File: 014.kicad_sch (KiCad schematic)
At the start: 19 parts, among them J14 USB2.0 Type C, U1 AM6232ASCGHAALWR, U6 TVS0500DRVR

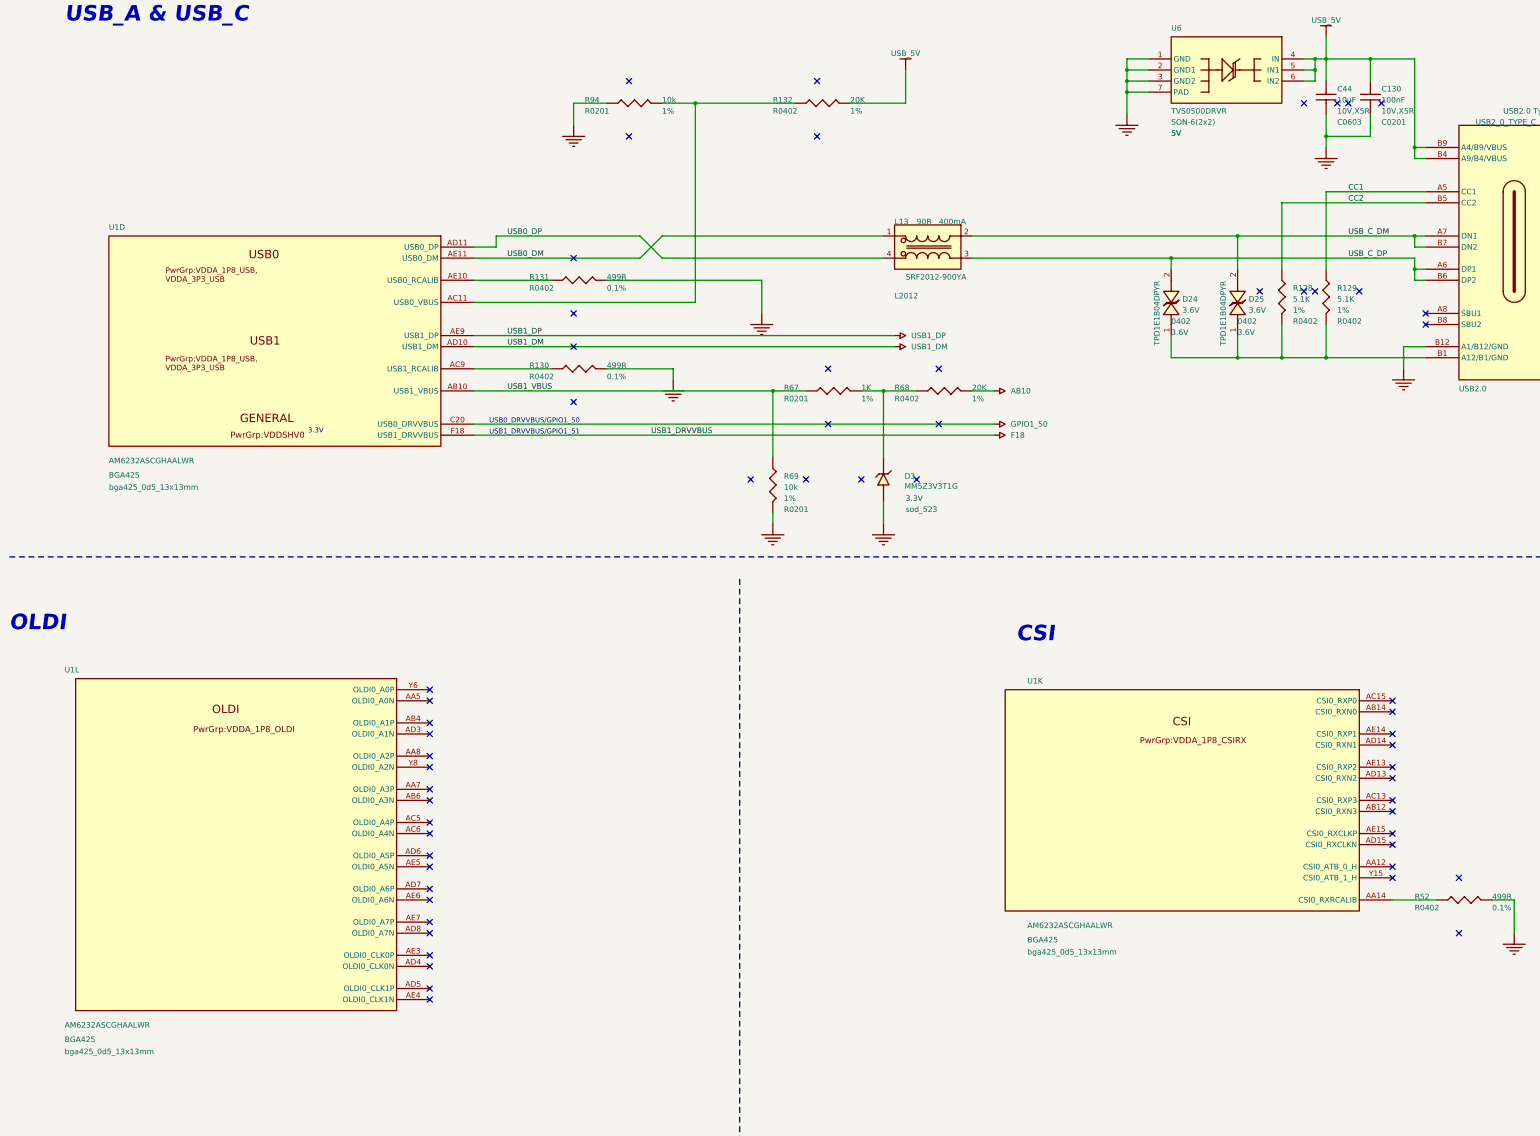
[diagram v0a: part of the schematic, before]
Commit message: Remove rando NCs added during conversion
Also a little tidying.

TODO: check junctions that may be missing. Noticed a few obvious ones
and corrected them already.

Signed-off-by: Michael Welling <mwelling79@gmail.com>
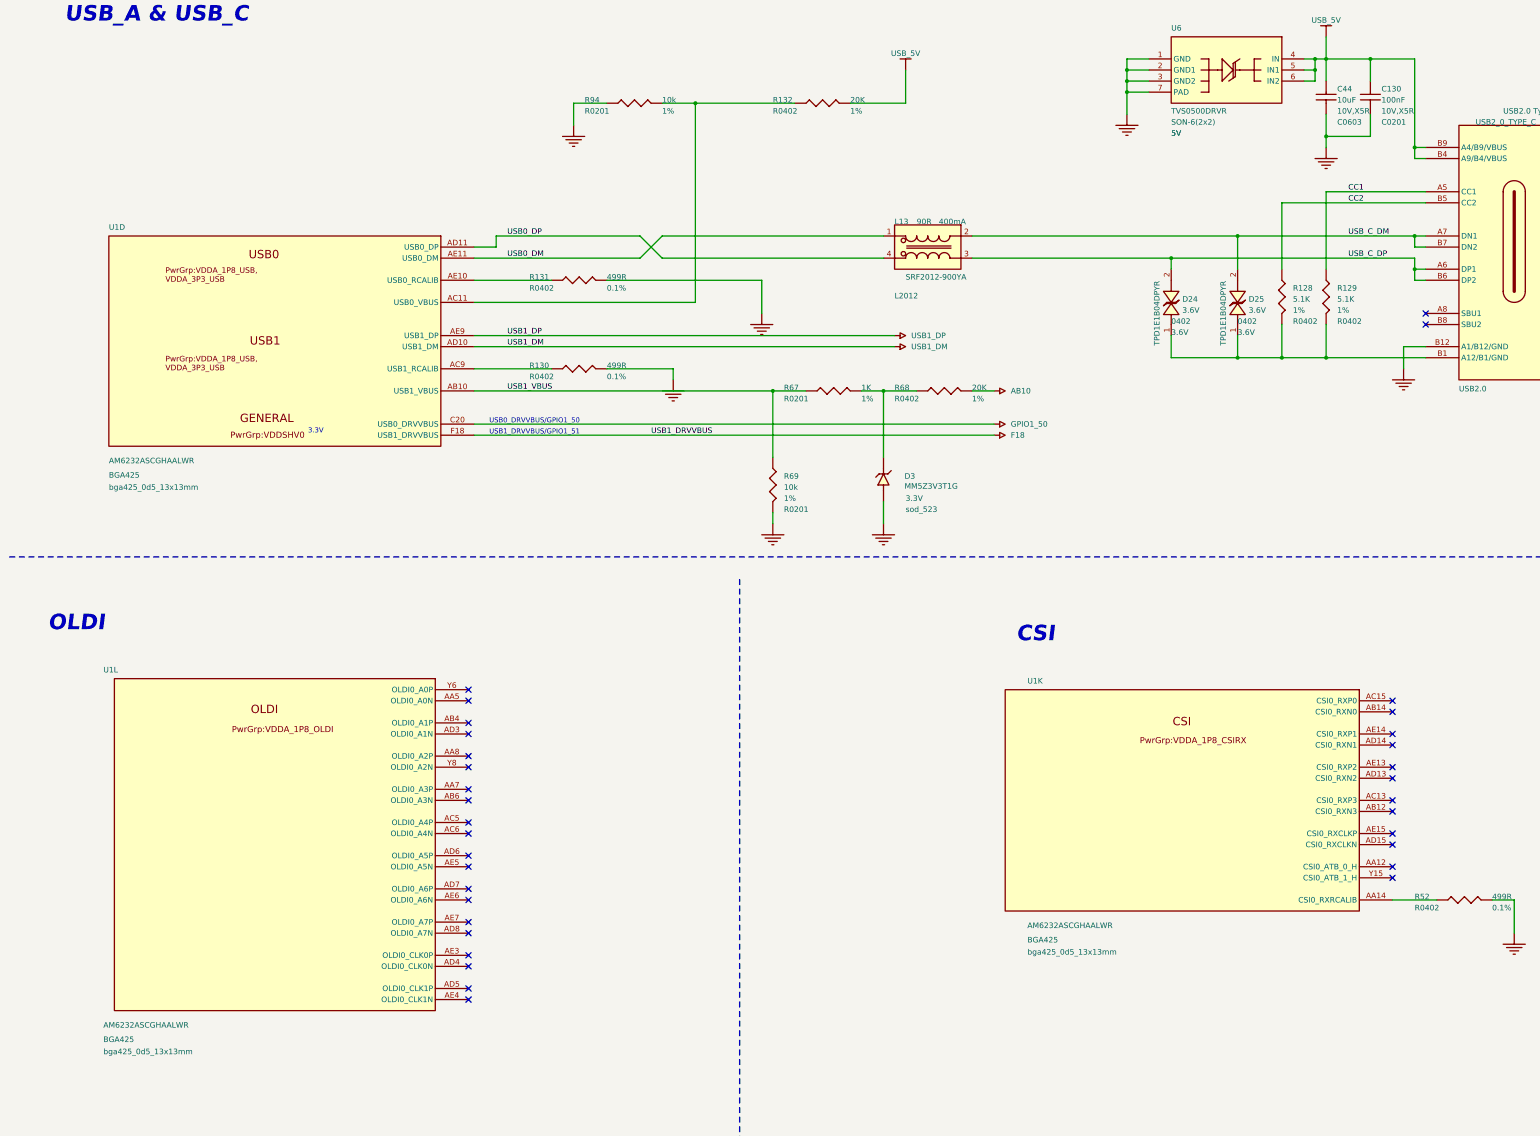
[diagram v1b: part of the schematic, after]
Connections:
- no-connect marks 60 -> 34
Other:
- moved on the sheet: U1L
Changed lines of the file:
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@@
 	)
 	(no_connect
-		(at 149.86 45.72)
-	)
-	(no_connect
-		(at 177.8 124.46)
-	)
-	(no_connect
 		(at 325.12 213.36)
 	)
@@
 	)
 	(no_connect
-		(at 220.98 99.06)
-	)
-	(no_connect
 		(at 325.12 190.5)
 	)
 	(no_connect
-		(at 104.14 180.34)
+		(at 113.03 180.34)
 	)
 	(no_connect
@@
 	)
 	(no_connect
-		(at 104.14 172.72)
+		(at 113.03 172.72)
 	)
 	(no_connect
-		(at 104.14 243.84)
-	)
-	(no_connect
-		(at 137.16 106.68)
+		(at 113.03 243.84)
 	)
 	(no_connect
@@
 	)
 	(no_connect
-		(at 104.14 233.68)
-	)
-	(no_connect
-		(at 340.36 228.6)
+		(at 113.03 233.68)
 	)
 	(no_connect
-		(at 322.58 38.1)
-	)
-	(no_connect
-		(at 104.14 213.36)
+		(at 113.03 213.36)
 	)
 	(no_connect
@@
 	)
 	(no_connect
-		(at 340.36 215.9)
-	)
-	(no_connect
-		(at 195.58 111.76)
-	)
-	(no_connect
-		(at 104.14 205.74)
-	)
-	(no_connect
-		(at 314.96 38.1)
-	)
-	(no_connect
-		(at 304.8 38.1)
+		(at 113.03 205.74)
 	)
 	(no_connect
-		(at 104.14 210.82)
+		(at 113.03 210.82)
 	)
 	(no_connect
-		(at 104.14 175.26)
-	)
-	(no_connect
-		(at 193.04 45.72)
+		(at 113.03 175.26)
 	)
 	(no_connect
@@
 	)
 	(no_connect
-		(at 104.14 198.12)
-	)
-	(no_connect
-		(at 215.9 124.46)
-	)
-	(no_connect
-		(at 220.98 111.76)
+		(at 113.03 198.12)
 	)
 	(no_connect
-		(at 104.14 226.06)
+		(at 113.03 226.06)
 	)
 	(no_connect
-		(at 104.14 182.88)
+		(at 113.03 182.88)
 	)
 	(no_connect
-		(at 104.14 203.2)
+		(at 113.03 203.2)
 	)
 	(no_connect
@@
 	)
 	(no_connect
-		(at 104.14 241.3)
+		(at 113.03 241.3)
 	)
 	(no_connect
-		(at 104.14 220.98)
+		(at 113.03 220.98)
 	)
 	(no_connect
-		(at 137.16 86.36)
+		(at 113.03 187.96)
 	)
 	(no_connect
-		(at 104.14 187.96)
-	)
-	(no_connect
-		(at 104.14 218.44)
-	)
-	(no_connect
-		(at 312.42 38.1)
-	)
-	(no_connect
-		(at 193.04 33.02)
+		(at 113.03 218.44)
 	)
 	(no_connect
@@
 	)
 	(no_connect
-		(at 104.14 195.58)
-	)
-	(no_connect
-		(at 104.14 190.5)
-	)
-	(no_connect
-		(at 190.5 124.46)
-	)
-	(no_connect
-		(at 149.86 33.02)
-	)
-	(no_connect
-		(at 195.58 99.06)
-	)
-	(no_connect
-		(at 137.16 73.66)
-	)
-	(no_connect
-		(at 203.2 124.46)
-	)
-	(no_connect
-		(at 304.8 81.28)
+		(at 113.03 195.58)
 	)
 	(no_connect
-		(at 104.14 236.22)
+		(at 113.03 190.5)
 	)
 	(no_connect
-		(at 104.14 228.6)
+		(at 113.03 236.22)
 	)
 	(no_connect
-		(at 307.34 81.28)
-	)
-	(no_connect
-		(at 294.64 81.28)
+		(at 113.03 228.6)
 	)
 	(no_connect
 		(at 325.12 208.28)
 	)
-	(no_connect
-		(at 137.16 93.98)
-	)
-	(no_connect
-		(at 317.5 81.28)
-	)
 	(wire
 		(pts
@@
 	(text "OLDI"
 		(exclude_from_sim no)
-		(at 7.62 159.512 0)
+		(at 16.51 159.512 0)
 		(effects
 			(font
@@
 	(symbol
 		(lib_id "pocketbeagle2-kicad-altium-import:root_0_mirrored_AM62x_BGA425")
-		(at 96.52 170.18 0)
+		(at 105.41 170.18 0)
 		(unit 12)
 		(exclude_from_sim no)
@@
 		(dnp no)
 		(property "Reference" "U1"
-			(at 20.32 168.91 0)
+			(at 29.21 168.91 0)
 			(effects
 				(font
@@
 		)
 		(property "Value" "AM6232ASCGHAALWR"
-			(at 20.32 250.444 0)
+			(at 29.21 250.444 0)
 			(effects
 				(font
@@
 		)
 		(property "Footprint" "bga425_0d5_13x13mm"
-			(at 96.52 170.18 0)
+			(at 105.41 170.18 0)
 			(effects
 				(font
@@
 		)
 		(property "Datasheet" ""
-			(at 96.52 170.18 0)
+			(at 105.41 170.18 0)
 			(effects
 				(font
@@
 		)
 		(property "Description" "SMD IC MPU;AM6232 Sitara Processor;BGA425"
-			(at 96.52 170.18 0)
+			(at 105.41 170.18 0)
 			(effects
 				(font
@@
 		)
 		(property "PCB FOOTPRINT" "bga425_0d5_13x13mm"
-			(at 20.32 256.54 0)
+			(at 29.21 256.54 0)
 			(effects
 				(font
@@
 		)
 		(property "STATUS" "BeaglePlay"
-			(at 73.66 297.18 0)
+			(at 82.55 297.18 0)
 			(effects
 				(font
@@
 		)
 		(property "MANUFACTURER" "TI"
-			(at 73.66 297.18 0)
+			(at 82.55 297.18 0)
 			(effects
 				(font
@@
 		)
 		(property "CLASS" "IC"
-			(at 73.66 297.18 0)
+			(at 82.55 297.18 0)
 			(effects
 				(font
@@
 		)
 		(property "ICA_MFR_NAME" ""
-			(at 73.66 297.18 0)
+			(at 82.55 297.18 0)
 			(effects
 				(font
@@
 		)
 		(property "ICA_PARTNUM" ""
-			(at 73.66 297.18 0)
+			(at 82.55 297.18 0)
 			(effects
 				(font
@@
 		)
 		(property "COMPANY PART STATUS" "BeaglePlay"
-			(at 73.66 297.18 0)
+			(at 82.55 297.18 0)
 			(effects
 				(font
@@
 		)
 		(property "PACKAGE SIZE" "BGA425"
-			(at 20.32 253.746 0)
+			(at 29.21 253.746 0)
 			(effects
 				(font
@@
 		)
 		(property "PN" "310011877"
-			(at 73.66 297.18 0)
+			(at 82.55 297.18 0)
 			(effects
 				(font
@@
 		)
 		(property "TEMPERATURE" "-40¡ãC to 105¡ãC"
-			(at 73.66 297.18 0)
+			(at 82.55 297.18 0)
 			(effects
 				(font
@@
 		)
 		(property "MANUFACTURER PART NUMBER" "AM6232ASCGHAALWR"
-			(at 73.66 297.18 0)
+			(at 82.55 297.18 0)
 			(effects
 				(font
